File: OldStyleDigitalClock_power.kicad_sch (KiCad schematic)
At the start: 22 parts, among them J1 USB_C_IN, J2 USB_A_OUT, J3 USB_A_OUT, U14 NA555P

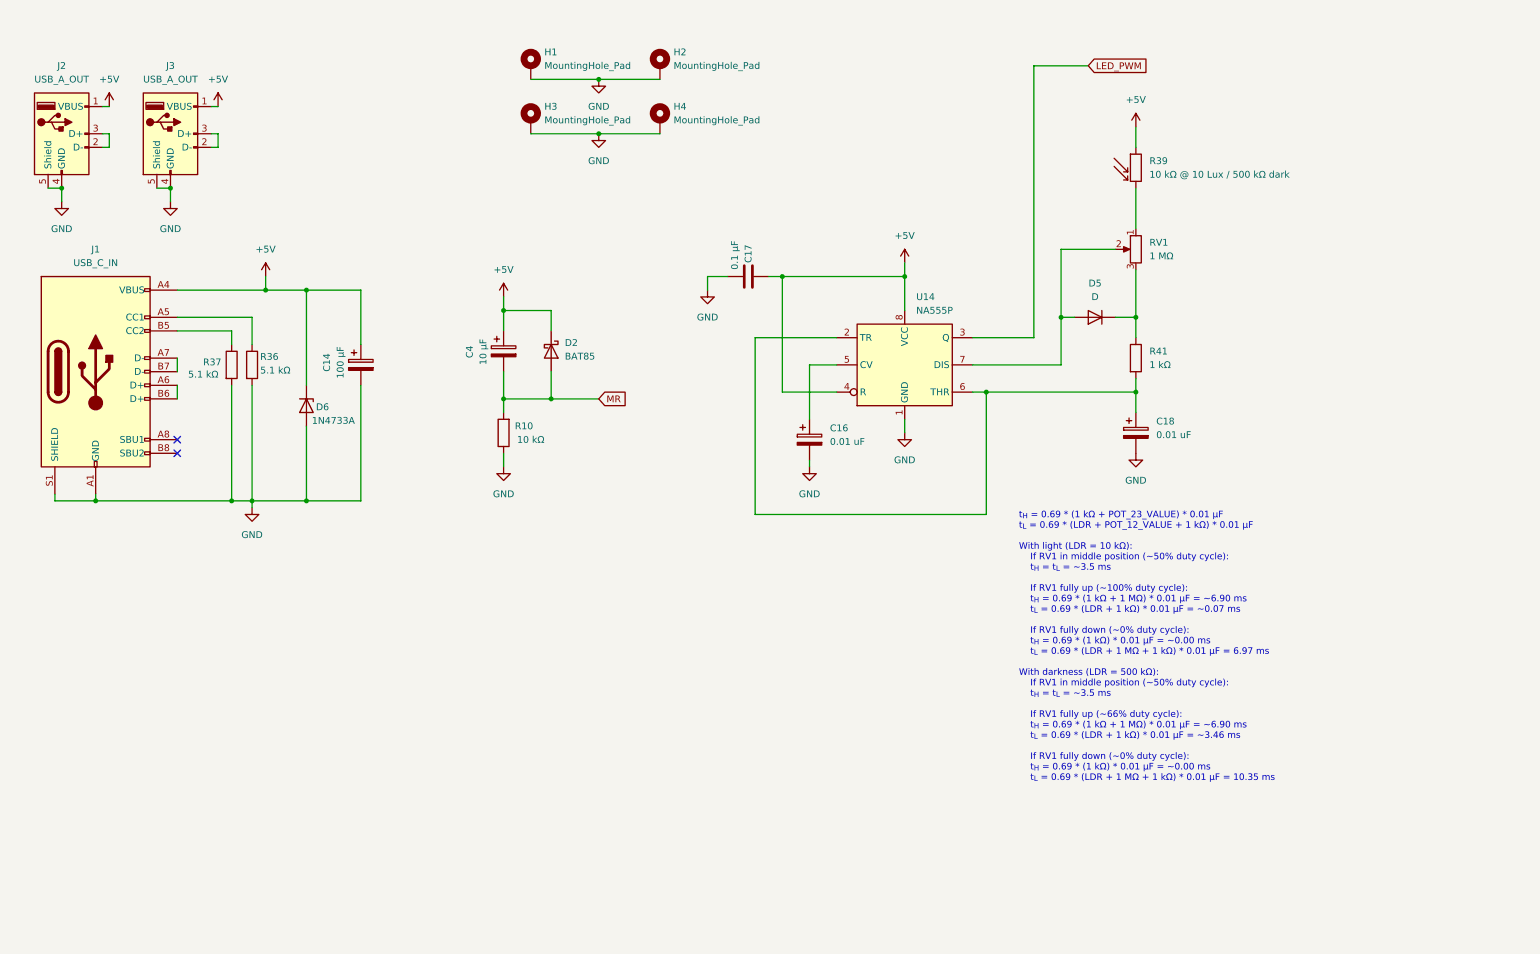
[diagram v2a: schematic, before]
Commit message: Using OR gates instead of diodes. Changed POT for 555
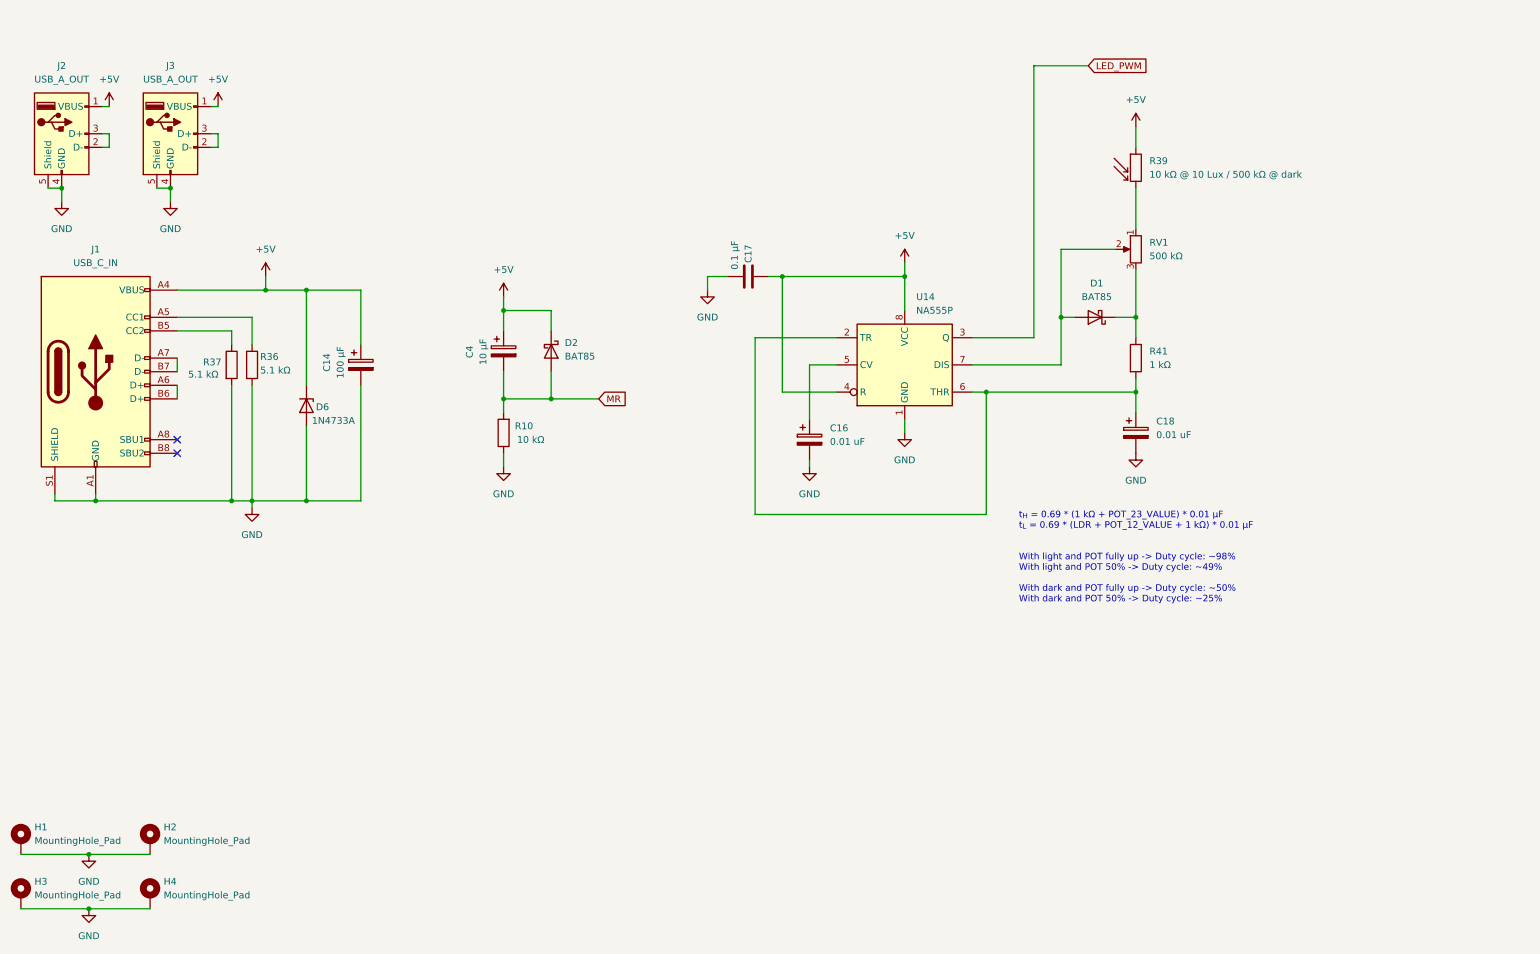
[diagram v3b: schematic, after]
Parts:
- removed D5: D, symbol Device:D
- added D1: BAT85, Diode_THT:D_DO-35_SOD27_P7.62mm_Horizontal, symbol Diode:BAT85
- R39: value 10 kΩ @ 10 Lux / 500 kΩ dark -> 10 kΩ @ 10 Lux / 500 kΩ @ dark
- RV1: value 1 MΩ -> 500 kΩ
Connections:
- net at R41.1, RV1.3: now also D1.1 (K)
- net at RV1.2, U14.7 (DIS): now also D1.2 (A)
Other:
- note added: "t_{H} = 0.69 * (1 kΩ + POT_23_VALUE) * 0.01 µF t_{L} = 0.69 * (LDR + POT_12_VALUE + 1 kΩ) * 0.01 µF With light and POT fully up -> Duty cycle: ~98% With light and POT 50% -> Duty cycle: ~49% With dark and POT fully up -> Duty cycle: ~50% With dark and POT 50% -> Duty cycle: ~25%"
- note removed: "t_{H} = 0.69 * (1 kΩ + POT_23_VALUE) * 0.01 µF t_{L} = 0.69 * (LDR + POT_12_VALUE + 1 kΩ) * 0.01 µF With light (LDR = 10 kΩ): If RV1 in middle position (~50% duty cycle): t_{H} = t_{L} = ~3.5 ms If RV1 fully up (~100% duty cycle): t_{H} = 0.69 * (1 kΩ + 1 MΩ) * 0.01 µF = ~6.90 ms t_{L} = 0.69 * (LDR + 1 kΩ) * 0.01 µF = ~0.07 ms If RV1 fully down (~0% duty cycle): t_{H} = 0.69 * (1 kΩ) * 0.01 µF =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"
- moved on the sheet: H1, H2, H3, H4
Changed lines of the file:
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@@
 		(company "Pasquale Lafiosca")
 	)
-	(text "t_{H} = 0.69 * (1 kΩ + POT_23_VALUE) * 0.01 µF\nt_{L} = 0.69 * (LDR + POT_12_VALUE + 1 kΩ) * 0.01 µF\n\nWith light (LDR = 10 kΩ):\n	If RV1 in middle position (~50% duty cycle):\n	t_{H} = t_{L} = ~3.5 ms\n\n	If RV1 fully up (~100% duty cycle):\n	t_{H} = 0.69 * (1 kΩ + 1 MΩ) * 0.01 µF = ~6.90 ms\n	t_{L} = 0.69 * (LDR + 1 kΩ) * 0.01 µF = ~0.07 ms\n\n	If RV1 fully down (~0% duty cycle):\n	t_{H} = 0.69 * (1 kΩ) * 0.01 µF = ~0.00 ms\n	t_{L} = 0.69 * (LDR + 1 MΩ + 1 kΩ) * 0.01 µF = 6.97 ms\n\nWith darkness (LDR = 500 kΩ):\n	If RV1 in middle position (~50% duty cycle):\n	t_{H} = t_{L} = ~3.5 ms\n\n	If RV1 fully up (~66% duty cycle):\n	t_{H} = 0.69 * (1 kΩ + 1 MΩ) * 0.01 µF = ~6.90 ms\n	t_{L} = 0.69 * (LDR + 1 kΩ) * 0.01 µF = ~3.46 ms\n\n	If RV1 fully down (~0% duty cycle):\n	t_{H} = 0.69 * (1 kΩ) * 0.01 µF = ~0.00 ms\n	t_{L} = 0.69 * (LDR + 1 MΩ + 1 kΩ) * 0.01 µF = 10.35 ms"
+	(text "t_{H} = 0.69 * (1 kΩ + POT_23_VALUE) * 0.01 µF\nt_{L} = 0.69 * (LDR + POT_12_VALUE + 1 kΩ) * 0.01 µF\n\n\nWith light and POT fully up -> Duty cycle: ~98%\nWith light and POT 50% -> Duty cycle: ~49%\n\nWith dark and POT fully up -> Duty cycle: ~50%\nWith dark and POT 50% -> Duty cycle: ~25%"
 		(exclude_from_sim no)
 		(at 211.836 111.252 0)
@@
 	)
 	(junction
-		(at 133.35 40.64)
+		(at 38.1 185.42)
 		(diameter 0)
 		(color 0 0 0 0)
 	)
 	(junction
-		(at 133.35 30.48)
+		(at 38.1 175.26)
 		(diameter 0)
 		(color 0 0 0 0)
@@
 	(wire
 		(pts
-			(xy 120.65 40.64) (xy 133.35 40.64)
+			(xy 25.4 185.42) (xy 38.1 185.42)
 		)
 		(stroke
@@
 	(wire
 		(pts
-			(xy 133.35 40.64) (xy 144.78 40.64)
+			(xy 38.1 185.42) (xy 49.53 185.42)
 		)
 		(stroke
@@
 	(wire
 		(pts
-			(xy 133.35 30.48) (xy 144.78 30.48)
+			(xy 38.1 175.26) (xy 49.53 175.26)
 		)
 		(stroke
@@
 	(wire
 		(pts
-			(xy 120.65 30.48) (xy 133.35 30.48)
+			(xy 25.4 175.26) (xy 38.1 175.26)
 		)
 		(stroke
@@
 	(symbol
 		(lib_id "power:GND")
-		(at 133.35 40.64 0)
+		(at 38.1 185.42 0)
 		(unit 1)
 		(exclude_from_sim no)
@@
 		(dnp no)
 		(property "Reference" "#PWR038"
-			(at 133.35 46.99 0)
+			(at 38.1 191.77 0)
 			(effects
 				(font
@@
 		)
 		(property "Value" "GND"
-			(at 133.35 45.72 0)
+			(at 38.1 190.5 0)
 			(effects
 				(font
@@
 		)
 		(property "Footprint" ""
-			(at 133.35 40.64 0)
+			(at 38.1 185.42 0)
 			(effects
 				(font
@@
 		)
 		(property "Datasheet" ""
-			(at 133.35 40.64 0)
+			(at 38.1 185.42 0)
 			(effects
 				(font
@@
 		)
 		(property "Description" ""
-			(at 133.35 40.64 0)
+			(at 38.1 185.42 0)
 			(effects
 				(font
@@
 	)
 	(symbol
-		(lib_id "Device:D")
-		(at 226.06 74.93 180)
-		(unit 1)
-		(exclude_from_sim no)
-		(in_bom yes)
-		(on_board yes)
-		(dnp no)
-		(fields_autoplaced yes)
-		(property "Reference" "D5"
-			(at 226.06 68.58 0)
-			(effects
-				(font
-					(size 1.27 1.27)
-				)
-			)
-		)
-		(property "Value" "D"
-			(at 226.06 71.12 0)
-			(effects
-				(font
-					(size 1.27 1.27)
-				)
-			)
-		)
-		(property "Footprint" ""
-			(at 226.06 74.93 0)
-			(effects
-				(font
-					(size 1.27 1.27)
-				)
-				(hide yes)
-			)
-		)
-		(property "Datasheet" "~"
-			(at 226.06 74.93 0)
-			(effects
-				(font
-					(size 1.27 1.27)
-				)
-				(hide yes)
-			)
-		)
-		(property "Description" "Diode"
-			(at 226.06 74.93 0)
-			(effects
-				(font
-					(size 1.27 1.27)
-				)
-				(hide yes)
-			)
-		)
-		(property "Sim.Device" "D"
-			(at 226.06 74.93 0)
-			(effects
-				(font
-					(size 1.27 1.27)
-				)
-				(hide yes)
-			)
-		)
-		(property "Sim.Pins" "1=K 2=A"
-			(at 226.06 74.93 0)
-			(effects
-				(font
-					(size 1.27 1.27)
-				)
-				(hide yes)
-			)
-		)
-		(pin "1"
-		)
-		(pin "2"
-		)
-		(instances
-			(project ""
-				(path "/a24f1d5b-eb61-47a3-9a92-6515e74f7a21/31b03831-3d01-49ef-8f86-173fa6c5d953"
-					(reference "D5")
-					(unit 1)
-				)
-			)
-		)
-	)
-	(symbol
 		(lib_id "Device:C_Polarized")
 		(at 233.68 96.52 0)
@@
 	(symbol
 		(lib_id "power:GND")
-		(at 133.35 30.48 0)
+		(at 38.1 175.26 0)
 		(unit 1)
 		(exclude_from_sim no)
@@
 		(dnp no)
 		(property "Reference" "#PWR023"
-			(at 133.35 36.83 0)
+			(at 38.1 181.61 0)
 			(effects
 				(font
@@
 		)
 		(property "Value" "GND"
-			(at 133.35 35.56 0)
+			(at 38.1 180.34 0)
 			(effects
 				(font
@@
 		)
 		(property "Footprint" ""
-			(at 133.35 30.48 0)
+			(at 38.1 175.26 0)
 			(effects
 				(font
@@
 		)
 		(property "Datasheet" ""
-			(at 133.35 30.48 0)
+			(at 38.1 175.26 0)
 			(effects
 				(font
@@
 		)
 		(property "Description" ""
-			(at 133.35 30.48 0)
+			(at 38.1 175.26 0)
 			(effects
 				(font
@@
 			)
 		)
-		(property "Value" "1 MΩ"
+		(property "Value" "500 kΩ"
 			(at 236.22 63.4999 0)
 			(effects
@@
 	(symbol
 		(lib_id "Mechanical:MountingHole_Pad")
-		(at 120.65 27.94 0)
+		(at 25.4 172.72 0)
 		(unit 1)
 		(exclude_from_sim no)
@@
 		(fields_autoplaced yes)
 		(property "Reference" "H1"
-			(at 123.19 25.3999 0)
+			(at 27.94 170.1799 0)
 			(effects
 				(font
@@
 		)
 		(property "Value" "MountingHole_Pad"
-			(at 123.19 27.9399 0)
+			(at 27.94 172.7199 0)
 			(effects
 				(font
@@
 		)
 		(property "Footprint" "MountingHole:MountingHole_2.2mm_M2_DIN965"
-			(at 120.65 27.94 0)
+			(at 25.4 172.72 0)
 			(effects
 				(font
@@
 		)
 		(property "Datasheet" "~"
-			(at 120.65 27.94 0)
+			(at 25.4 172.72 0)
 			(effects
 				(font
@@
 		)
 		(property "Description" "Mounting Hole with connection"
-			(at 120.65 27.94 0)
+			(at 25.4 172.72 0)
 			(effects
 				(font
@@
 	(symbol
 		(lib_id "Mechanical:MountingHole_Pad")
-		(at 144.78 27.94 0)
+		(at 49.53 172.72 0)
 		(unit 1)
 		(exclude_from_sim no)
@@
 		(fields_autoplaced yes)
 		(property "Reference" "H2"
-			(at 147.32 25.3999 0)
+			(at 52.07 170.1799 0)
 			(effects
 				(font
@@
 		)
 		(property "Value" "MountingHole_Pad"
-			(at 147.32 27.9399 0)
+			(at 52.07 172.7199 0)
 			(effects
 				(font
@@
 		)
 		(property "Footprint" "MountingHole:MountingHole_2.2mm_M2_DIN965"
-			(at 144.78 27.94 0)
+			(at 49.53 172.72 0)
 			(effects
 				(font
@@
 		)
 		(property "Datasheet" "~"
-			(at 144.78 27.94 0)
+			(at 49.53 172.72 0)
 			(effects
 				(font
@@
 		)
 		(property "Description" "Mounting Hole with connection"
-			(at 144.78 27.94 0)
+			(at 49.53 172.72 0)
 			(effects
 				(font
@@
 			)
 		)
-		(property "Value" "10 kΩ @ 10 Lux / 500 kΩ dark"
+		(property "Value" "10 kΩ @ 10 Lux / 500 kΩ @ dark"
 			(at 236.22 48.2599 0)
 			(effects
@@
 	)
 	(symbol
+		(lib_id "Diode:BAT85")
+		(at 226.06 74.93 180)
+		(unit 1)
+		(exclude_from_sim no)
+		(in_bom yes)
+		(on_board yes)
+		(dnp no)
+		(fields_autoplaced yes)
+		(property "Reference" "D1"
+			(at 226.3775 68.58 0)
+			(effects
+				(font
+					(size 1.27 1.27)
+				)
+			)
+		)
+		(property "Value" "BAT85"
+			(at 226.3775 71.12 0)
+			(effects
+				(font
+					(size 1.27 1.27)
+				)
+			)
+		)
+		(property "Footprint" "Diode_THT:D_DO-35_SOD27_P7.62mm_Horizontal"
+			(at 226.06 70.485 0)
+			(effects
+				(font
+					(size 1.27 1.27)
+				)
+				(hide yes)
+			)
+		)
+		(property "Datasheet" "https://assets.nexperia.com/documents/data-sheet/BAT85.pdf"
+			(at 226.06 74.93 0)
+			(effects
+				(font
+					(size 1.27 1.27)
+				)
+				(hide yes)
+			)
+		)
+		(property "Description" ""
+			(at 226.06 74.93 0)
+			(effects
+				(font
+					(size 1.27 1.27)
+				)
+			)
+		)
+		(pin "1"
+		)
+		(pin "2"
+		)
+		(instances
+			(project "OldStyleDigitalClock"
+				(path "/a24f1d5b-eb61-47a3-9a92-6515e74f7a21/31b03831-3d01-49ef-8f86-173fa6c5d953"
+					(reference "D1")
+					(unit 1)
+				)
+			)
+		)
+	)
+	(symbol
 		(lib_id "power:GND")
 		(at 53.34 53.34 0)
@@
 	(symbol
 		(lib_id "Mechanical:MountingHole_Pad")
-		(at 144.78 38.1 0)
+		(at 49.53 182.88 0)
 		(unit 1)
 		(exclude_from_sim no)
@@
 		(fields_autoplaced yes)
 		(property "Reference" "H4"
-			(at 147.32 35.5599 0)
+			(at 52.07 180.3399 0)
 			(effects
 				(font
@@
 		)
 		(property "Value" "MountingHole_Pad"
-			(at 147.32 38.0999 0)
+			(at 52.07 182.8799 0)
 			(effects
 				(font
@@
 		)
 		(property "Footprint" "MountingHole:MountingHole_2.2mm_M2_DIN965"
-			(at 144.78 38.1 0)
+			(at 49.53 182.88 0)
 			(effects
 				(font
@@
 		)
 		(property "Datasheet" "~"
-			(at 144.78 38.1 0)
+			(at 49.53 182.88 0)
 			(effects
 				(font
@@
 		)
 		(property "Description" "Mounting Hole with connection"
-			(at 144.78 38.1 0)
+			(at 49.53 182.88 0)
 			(effects
 				(font
@@
 	(symbol
 		(lib_id "Mechanical:MountingHole_Pad")
-		(at 120.65 38.1 0)
+		(at 25.4 182.88 0)
 		(unit 1)
 		(exclude_from_sim no)
@@
 		(fields_autoplaced yes)
 		(property "Reference" "H3"
-			(at 123.19 35.5599 0)
+			(at 27.94 180.3399 0)
 			(effects
 				(font
@@
 		)
 		(property "Value" "MountingHole_Pad"
-			(at 123.19 38.0999 0)
+			(at 27.94 182.8799 0)
 			(effects
 				(font
@@
 		)
 		(property "Footprint" "MountingHole:MountingHole_2.2mm_M2_DIN965"
-			(at 120.65 38.1 0)
+			(at 25.4 182.88 0)
 			(effects
 				(font
@@
 		)
 		(property "Datasheet" "~"
-			(at 120.65 38.1 0)
+			(at 25.4 182.88 0)
 			(effects
 				(font
@@
 		)
 		(property "Description" "Mounting Hole with connection"
-			(at 120.65 38.1 0)
+			(at 25.4 182.88 0)
 			(effects
 				(font
